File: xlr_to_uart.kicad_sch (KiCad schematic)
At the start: 12 parts, among them J13 XLR A/B, J14 Conn_01x04_Socket, J15 XLR3, J16 XLR3, J4 Conn_01x04_Socket, U8 MAX485E

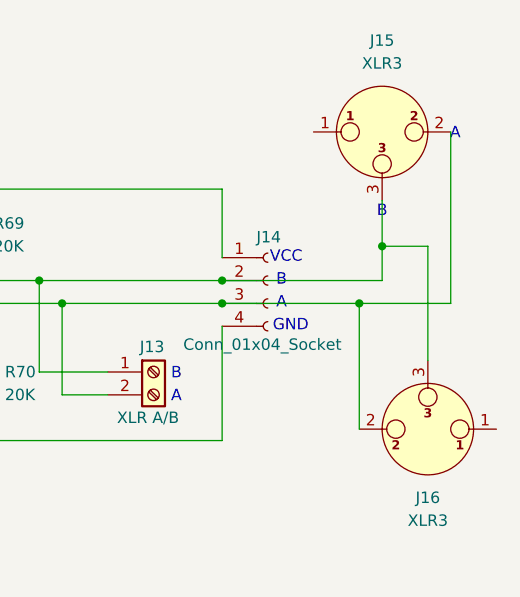
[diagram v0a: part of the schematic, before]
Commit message: replace extended components with basic components.
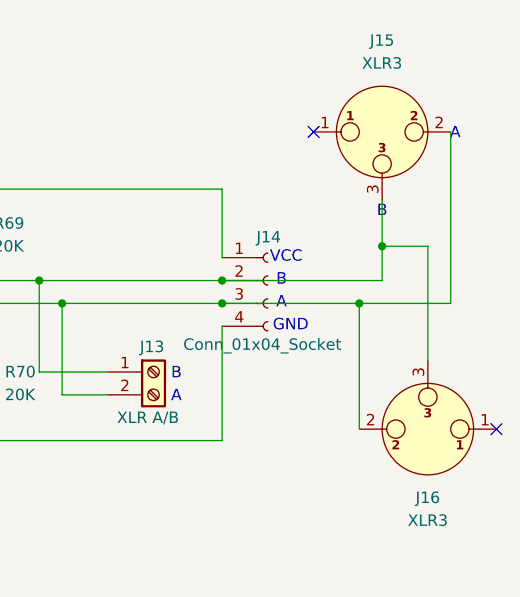
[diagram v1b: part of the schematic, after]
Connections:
- no-connect marks 0 -> 2
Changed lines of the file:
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@@
 		(color 0 0 0 0)
+	)
+	(no_connect
+		(at 161.29 54.61)
+	)
+	(no_connect
+		(at 181.61 87.63)
 	)
 	(wire
